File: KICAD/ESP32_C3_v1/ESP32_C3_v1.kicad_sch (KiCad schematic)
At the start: 1 part, among them U1 ESP32-C3-DevKitC-02

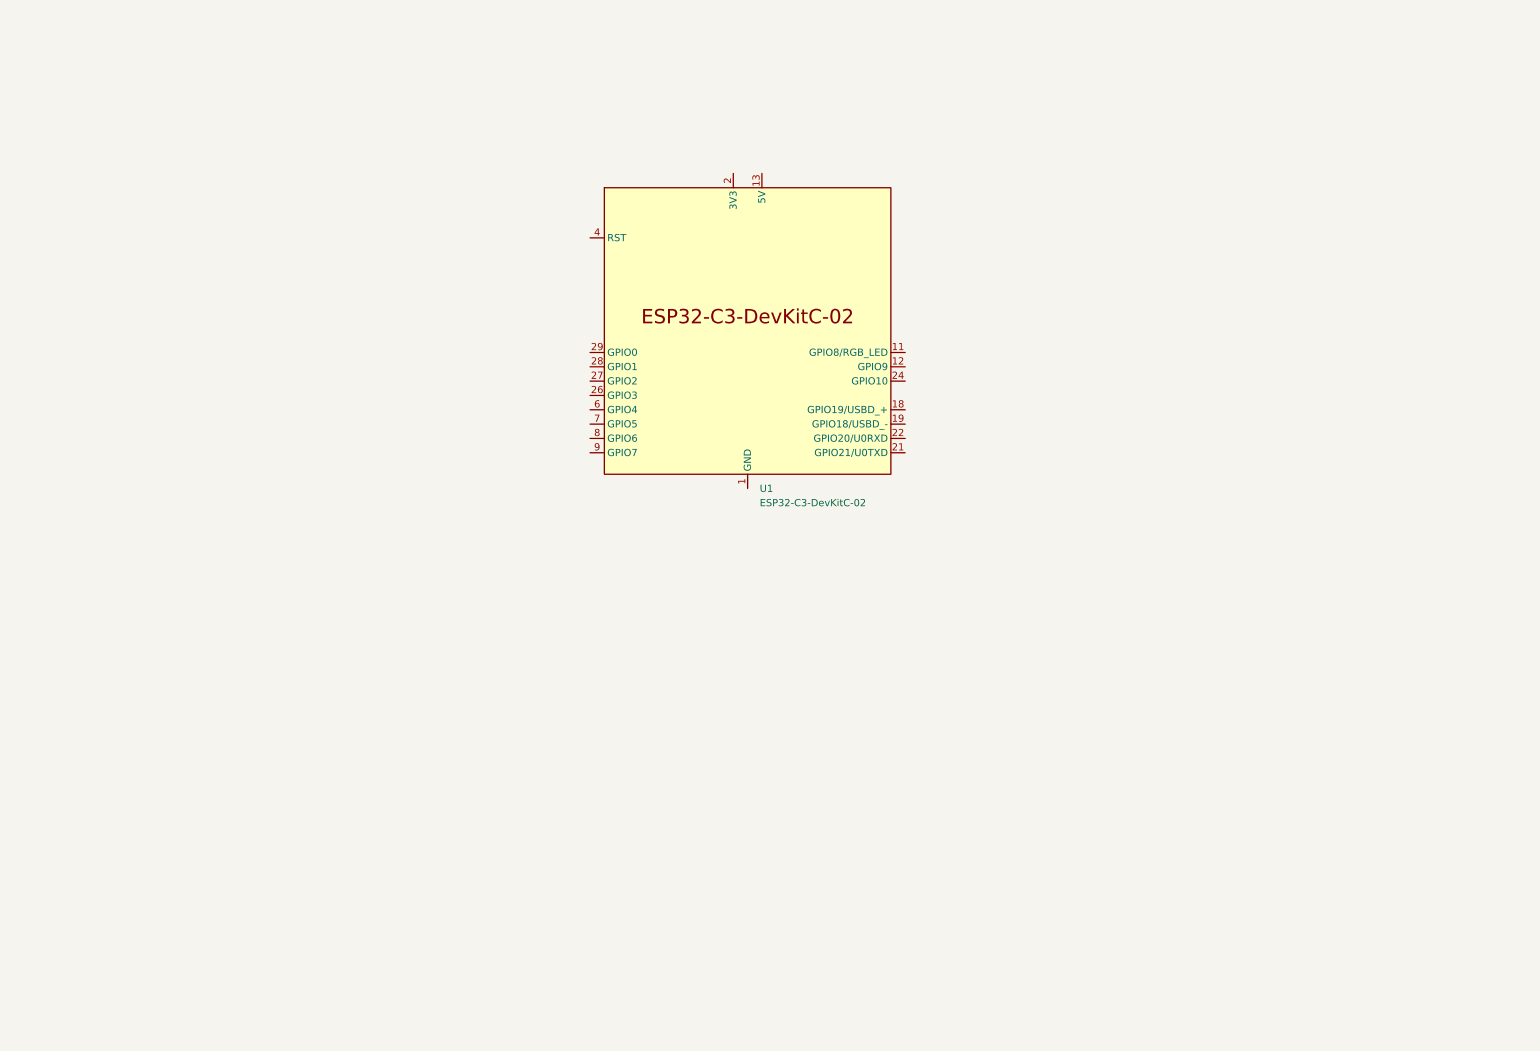
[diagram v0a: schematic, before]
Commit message: Add cleaned ESP32-C3 harness KiCad project
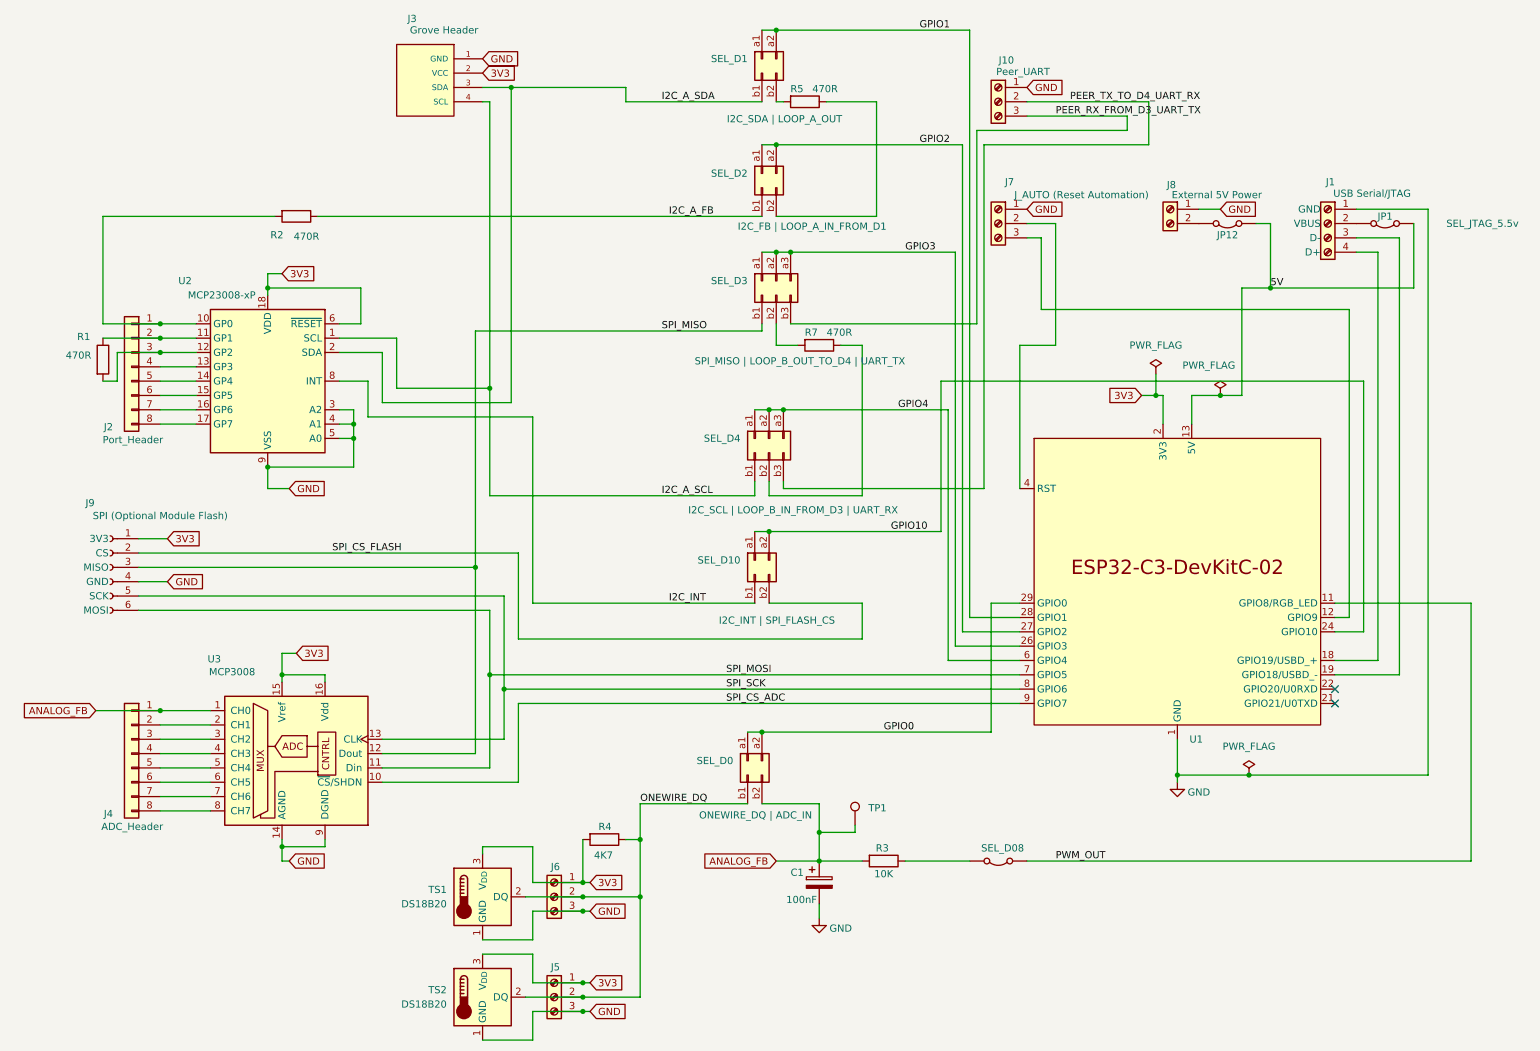
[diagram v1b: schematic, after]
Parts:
- removed U1: ESP32-C3-DevKitC-02, PCM_Espressif:ESP32-C3-DevKitC-02, symbol PCM_Espressif:ESP32-C3-DevKitC-02
- added C1: 100nF, ESP32_C3_Harness:C_Disc_D4.7mm_W2.5mm_P5.00mm, symbol ESP32_C3_Harness:C_Polarized
- added J1: USB Serial/JTAG, ESP32_C3_Harness:TerminalBlock_Phoenix_MPT-0,5-4-2.54_1x04_P2.54mm_Horizontal, symbol ESP32_C3_Harness:Screw_Terminal_01x04
- added J10: Peer_UART, ESP32_C3_Harness:TerminalBlock_Phoenix_MPT-0,5-3-2.54_1x03_P2.54mm_Horizontal, symbol ESP32_C3_Harness:Screw_Terminal_01x03
- added J2: Port_Header, ESP32_C3_Harness:PinHeader_1x08_P2.54mm_Vertical, symbol ESP32_C3_Harness:Conn_01x08
- added J3: Grove Header, ESP32_C3_Harness:Grove_1x04_P2mm(SEEED_110990030), symbol ESP32_C3_Harness:Grove_Female_Header_-_DIP-4P-2.0mm
- added J4: ADC_Header, ESP32_C3_Harness:PinHeader_1x08_P2.54mm_Vertical, symbol ESP32_C3_Harness:Conn_01x08
- added J5, J6: Screw_Terminal_01x03, ESP32_C3_Harness:TerminalBlock_Phoenix_MPT-0,5-3-2.54_1x03_P2.54mm_Horizontal, symbol ESP32_C3_Harness:Screw_Terminal_01x03
- added J7: J_AUTO (Reset Automation), ESP32_C3_Harness:TerminalBlock_Phoenix_MPT-0,5-3-2.54_1x03_P2.54mm_Horizontal, symbol ESP32_C3_Harness:Screw_Terminal_01x03
- added J8: External 5V Power, ESP32_C3_Harness:TerminalBlock_Phoenix_MPT-0,5-2-2.54_1x02_P2.54mm_Horizontal, symbol ESP32_C3_Harness:Screw_Terminal_01x02
- added J9: SPI (Optional Module Flash), ESP32_C3_Harness:PinSocket_1x06_P2.54mm_Vertical, symbol ESP32_C3_Harness:Conn_01x06_Socket
- added JP1: SEL_JTAG_5.5v, ESP32_C3_Harness:PinHeader_1x02_P2.54mm_Vertical, symbol ESP32_C3_Harness:Jumper_2_Open
- added JP12: EXT_5V_SHUNT, ESP32_C3_Harness:PinHeader_1x02_P2.54mm_Vertical, symbol ESP32_C3_Harness:Jumper_2_Open
- added R1, R2, R5, R7: 470R, ESP32_C3_Harness:R_Axial_DIN0411_L9.9mm_D3.6mm_P5.08mm_Vertical, symbol ESP32_C3_Harness:Resistor
- added R3: 10K, ESP32_C3_Harness:R_Axial_DIN0411_L9.9mm_D3.6mm_P5.08mm_Vertical, symbol ESP32_C3_Harness:Resistor
- added R4: 4K7, ESP32_C3_Harness:R_Axial_DIN0411_L9.9mm_D3.6mm_P5.08mm_Vertical, symbol ESP32_C3_Harness:Resistor
- added SEL_D0: ONEWIRE_DQ | ADC_IN, ESP32_C3_Harness:PinHeader_2x02_P2.54mm_Vertical, symbol ESP32_C3_Harness:Conn_02x02_Row_Letter_First
- added SEL_D08: PWM_OUT, ESP32_C3_Harness:PinHeader_1x02_P2.54mm_Vertical, symbol ESP32_C3_Harness:Jumper_2_Open
- added SEL_D1: I2C_SDA | LOOP_A_OUT, ESP32_C3_Harness:PinHeader_2x02_P2.54mm_Vertical, symbol ESP32_C3_Harness:Conn_02x02_Row_Letter_First
- added SEL_D10: I2C_INT | SPI_FLASH_CS, ESP32_C3_Harness:PinHeader_2x02_P2.54mm_Vertical, symbol ESP32_C3_Harness:Conn_02x02_Row_Letter_First
- added SEL_D2: I2C_FB | LOOP_A_IN_FROM_D1, ESP32_C3_Harness:PinHeader_2x02_P2.54mm_Vertical, symbol ESP32_C3_Harness:Conn_02x02_Row_Letter_First
- added SEL_D3: SPI_MISO | LOOP_B_OUT_TO_D4 | UART_TX, ESP32_C3_Harness:PinHeader_2x03_P2.54mm_Vertical, symbol ESP32_C3_Harness:Conn_02x03_Row_Letter_First
- added SEL_D4: I2C_SCL | LOOP_B_IN_FROM_D3 | UART_RX, ESP32_C3_Harness:PinHeader_2x03_P2.54mm_Vertical, symbol ESP32_C3_Harness:Conn_02x03_Row_Letter_First
- added TP1: ANALOG_FB, ESP32_C3_Harness:PinHeader_1x01_P2.54mm_Vertical, symbol ESP32_C3_Harness:TestPoint
- added TS1, TS2: DS18B20, Package_TO_SOT_THT:TO-92_Inline, symbol ESP32_C3_Harness:DS18B20
- added U1: ESP32-C3-DevKitC-02, ESP32_C3_Harness:ESP32-C3-DevKitC-02, symbol ESP32_C3_Harness:ESP32-C3-DevKitC-02
- added U2: MCP23008-xP, ESP32_C3_Harness:DIP-18_W7.62mm, symbol ESP32_C3_Harness:MCP23008-xP
- added U3: MCP3008, ESP32_C3_Harness:DIP-16_W7.62mm, symbol ESP32_C3_Harness:MCP3008
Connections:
- net 3V3: now also J3.2 (VCC), J5.1 (Pin_1), J6.1 (Pin_1), J9.1 (3V3), R4.2, TS1.3 (V_{DD}), TS2.3 (V_{DD}), U1.2 (3V3), U1.3 (3V3), U2.18 (VDD), U2.6 (~{RESET}), U3.15 (Vref), U3.16 (Vdd)
- net 5V: now also JP1.1 (A), JP12.1 (A), U1.13 (5V), U1.14 (5V)
- new net: J1.2 (VBUS), JP1.2 (B)
- new net: J1.3 (D-), U1.19 (GPIO18/USBD_-)
- new net: J1.4 (D+), U1.18 (GPIO19/USBD_+)
- new net: R7.2, SEL_D3.b2 (Pin_b2)
- new net: J2.2 (Pin_2), R1.1, U2.11 (GP1)
- new net: J2.3 (Pin_3), R1.2, U2.12 (GP2)
- new net: R5.1, SEL_D2.b2 (Pin_b2)
- new net: R5.2, SEL_D1.b2 (Pin_b2)
- new net: R7.1, SEL_D4.b2 (Pin_b2)
- new net: J2.1 (Pin_1), R2.2, U2.10 (GP0)
- new net: J2.4 (Pin_4), U2.13 (GP3)
- new net: J2.5 (Pin_5), U2.14 (GP4)
- new net: J2.6 (Pin_6), U2.15 (GP5)
- new net: J2.7 (Pin_7), U2.16 (GP6)
- new net: J2.8 (Pin_8), U2.17 (GP7)
- new net: J4.2 (Pin_2), U3.2 (CH1)
- new net: J4.3 (Pin_3), U3.3 (CH2)
- new net: J4.4 (Pin_4), U3.4 (CH3)
- new net: J4.5 (Pin_5), U3.5 (CH4)
- new net: J4.6 (Pin_6), U3.6 (CH5)
- new net: J4.7 (Pin_7), U3.7 (CH6)
- new net: J4.8 (Pin_8), U3.8 (CH7)
- new net: R3.1, SEL_D08.2 (B)
- new net: J7.3 (Pin_3), U1.12 (GPIO9)
- new net: J7.2 (Pin_2), U1.4 (RST)
- new net: J8.2 (Pin_2), JP12.2 (B)
- new net ANALOG_FB: C1.1, J4.1 (Pin_1), R3.2, SEL_D0.b2 (Pin_b2), TP1.1, U3.1 (CH0)
- new net GND: C1.2, J1.1 (GND), J10.1 (Pin_1), J3.1 (GND), J5.3 (Pin_3), J6.3 (Pin_3), J7.1 (Pin_1), J8.1 (Pin_1), J9.4 (GND), TS1.1 (GND), TS2.1 (GND), U1.1 (GND), U1.10 (GND), U1.15 (GND), U1.16 (GND), U1.17 (GND), U1.20 (GND), U1.23 (GND), U1.25 (GND), U1.30 (GND), U1.5 (GND), U2.3 (A2), U2.4 (A1), U2.5 (A0), U2.9 (VSS), U3.14 (AGND), U3.9 (DGND)
- new net GPIO0: SEL_D0.a1 (Pin_a1), SEL_D0.a2 (Pin_a2), U1.29 (GPIO0)
- new net GPIO1: SEL_D1.a1 (Pin_a1), SEL_D1.a2 (Pin_a2), U1.28 (GPIO1)
- new net GPIO10: SEL_D10.a1 (Pin_a1), SEL_D10.a2 (Pin_a2), U1.24 (GPIO10)
- new net GPIO2: SEL_D2.a1 (Pin_a1), SEL_D2.a2 (Pin_a2), U1.27 (GPIO2)
- new net GPIO3: SEL_D3.a1 (Pin_a1), SEL_D3.a2 (Pin_a2), SEL_D3.a3 (Pin_a3), U1.26 (GPIO3)
- new net GPIO4: SEL_D4.a1 (Pin_a1), SEL_D4.a2 (Pin_a2), SEL_D4.a3 (Pin_a3), U1.6 (GPIO4)
- new net I2C_A_FB: R2.1, SEL_D2.b1 (Pin_b1)
- new net I2C_A_SCL: J3.4 (SCL), SEL_D4.b1 (Pin_b1), U2.1 (SCL)
- new net I2C_A_SDA: J3.3 (SDA), SEL_D1.b1 (Pin_b1), U2.2 (SDA)
- new net I2C_INT: SEL_D10.b1 (Pin_b1), U2.8 (INT)
- new net ONEWIRE_DQ: J5.2 (Pin_2), J6.2 (Pin_2), R4.1, SEL_D0.b1 (Pin_b1), TS1.2 (DQ), TS2.2 (DQ)
- new net PEER_RX_FROM_D3_UART_TX: J10.3 (Pin_3), SEL_D3.b3 (Pin_b3)
- new net PEER_TX_TO_D4_UART_RX: J10.2 (Pin_2), SEL_D4.b3 (Pin_b3)
- new net PWM_OUT: SEL_D08.1 (A), U1.11 (GPIO8/RGB_LED)
- new net SPI_CS_ADC: U1.9 (GPIO7), U3.10 (~{CS}/SHDN)
- new net SPI_CS_FLASH: J9.2 (CS), SEL_D10.b2 (Pin_b2)
- new net SPI_MISO: J9.3 (MISO), SEL_D3.b1 (Pin_b1), U3.12 (Dout)
- new net SPI_MOSI: J9.6 (MOSI), U1.7 (GPIO5), U3.11 (Din)
- new net SPI_SCK: J9.5 (SCK), U1.8 (GPIO6), U3.13 (CLK)
- no-connect marks 0 -> 2
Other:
- company: (none) -> SimonGAndrews
- title: (none) -> Espruino ESP32_C3 Test Harness

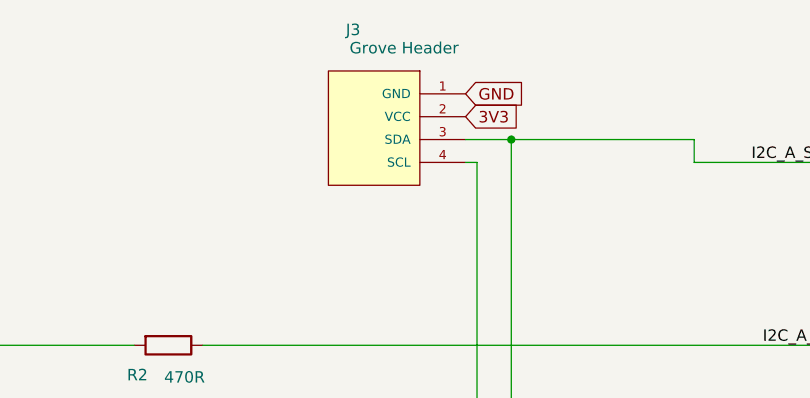
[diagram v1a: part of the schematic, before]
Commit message: Add ESP32-C3 harness v1 PCB draft
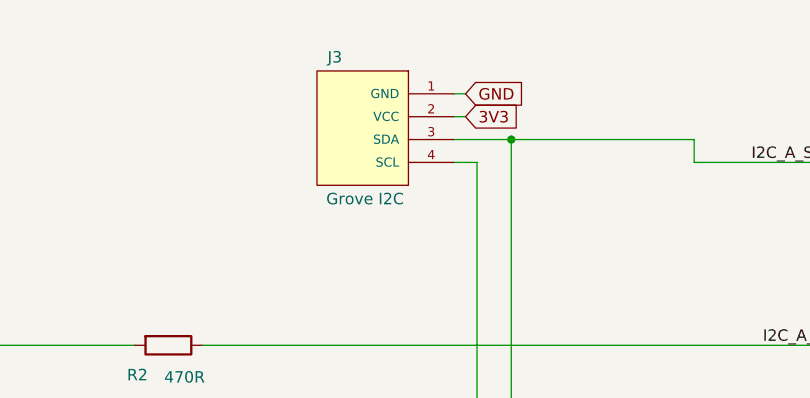
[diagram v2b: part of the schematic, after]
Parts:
- J3: value Grove Header -> Grove I2C
- JP12: value EXT_5V_SHUNT -> EXT_5V
- SEL_D0, SEL_D1, SEL_D10, SEL_D2: footprint ESP32_C3_Harness:PinHeader_2x02_P2.54mm_Vertical -> ESP32_C3_Harness:PinHeader_2x02_RowLetter_P2.54mm_Vertical
- SEL_D3, SEL_D4: footprint ESP32_C3_Harness:PinHeader_2x03_P2.54mm_Vertical -> ESP32_C3_Harness:PinHeader_2x03_RowLetter_P2.54mm_Vertical
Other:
- moved on the sheet: J3
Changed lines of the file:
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@@
 	(wire
 		(pts
+			(xy 96.52 21.59) (xy 97.79 21.59)
+		)
+		(stroke
+			(width 0)
+			(type default)
+		)
+	)
+	(wire
+		(pts
 			(xy 62.23 128.27) (xy 62.23 129.54)
 		)
@@
 	(wire
 		(pts
-			(xy 97.79 26.67) (xy 99.06 26.67)
+			(xy 96.52 26.67) (xy 99.06 26.67)
 		)
 		(stroke
@@
 	(wire
 		(pts
+			(xy 96.52 19.05) (xy 97.79 19.05)
+		)
+		(stroke
+			(width 0)
+			(type default)
+		)
+	)
+	(wire
+		(pts
 			(xy 232.41 59.69) (xy 237.49 59.69)
 		)
@@
 	(wire
 		(pts
-			(xy 97.79 24.13) (xy 102.87 24.13)
+			(xy 96.52 24.13) (xy 102.87 24.13)
 		)
 		(stroke
@@
 			)
 		)
-		(property "Footprint" "ESP32_C3_Harness:PinHeader_2x03_P2.54mm_Vertical"
+		(property "Footprint" "ESP32_C3_Harness:PinHeader_2x03_RowLetter_P2.54mm_Vertical"
 			(at 149.86 58.42 0)
 			(effects
@@
 			)
 		)
-		(property "Footprint" "ESP32_C3_Harness:PinHeader_2x02_P2.54mm_Vertical"
+		(property "Footprint" "ESP32_C3_Harness:PinHeader_2x02_RowLetter_P2.54mm_Vertical"
 			(at 147.32 39.37 0)
 			(effects
@@
 			)
 		)
-		(property "Footprint" "ESP32_C3_Harness:PinHeader_2x02_P2.54mm_Vertical"
+		(property "Footprint" "ESP32_C3_Harness:PinHeader_2x02_RowLetter_P2.54mm_Vertical"
 			(at 147.32 19.05 0)
 			(effects
@@
 			)
 		)
-		(property "Footprint" "ESP32_C3_Harness:PinHeader_2x03_P2.54mm_Vertical"
+		(property "Footprint" "ESP32_C3_Harness:PinHeader_2x03_RowLetter_P2.54mm_Vertical"
 			(at 148.59 86.36 0)
 			(effects
@@
 			)
 		)
-		(property "Footprint" "ESP32_C3_Harness:PinHeader_2x02_P2.54mm_Vertical"
+		(property "Footprint" "ESP32_C3_Harness:PinHeader_2x02_RowLetter_P2.54mm_Vertical"
 			(at 144.78 143.51 0)
 			(effects
@@
 	(symbol
 		(lib_id "ESP32_C3_Harness:Grove_Female_Header_-_DIP-4P-2.0mm")
-		(at 87.63 21.59 0)
+		(at 86.36 21.59 0)
 		(mirror y)
 		(unit 1)
@@
 		(dnp no)
 		(property "Reference" "J3"
-			(at 86.106 11.938 0)
+			(at 84.074 14.986 0)
 			(effects
 				(font
@@
 			)
 		)
-		(property "Value" "Grove Header"
-			(at 97.028 13.97 0)
+		(property "Value" "Grove I2C"
+			(at 90.932 30.734 0)
 			(effects
 				(font
@@
 		)
 		(property "Footprint" "ESP32_C3_Harness:Grove_1x04_P2mm(SEEED_110990030)"
-			(at 87.122 8.382 0)
+			(at 85.852 8.382 0)
 			(effects
 				(font
@@
 		)
 		(property "Datasheet" "https://www.snapeda.com/parts/110990030%2010PCS/PACK/Seeed+Studio/view-part/?ref=snap"
-			(at 53.086 12.954 0)
+			(at 51.816 12.954 0)
 			(effects
 				(font
@@
 		)
 		(property "Description" "Grove_Female_Header  DIP-4P-2.0mm"
-			(at 80.772 10.668 0)
+			(at 79.502 10.668 0)
 			(effects
 				(font
@@
 			)
 		)
-		(property "Value" "EXT_5V_SHUNT"
+		(property "Value" "EXT_5V"
 			(at 229.87 39.37 90)
 			(effects
@@
 			)
 		)
-		(property "Footprint" "ESP32_C3_Harness:PinHeader_2x02_P2.54mm_Vertical"
+		(property "Footprint" "ESP32_C3_Harness:PinHeader_2x02_RowLetter_P2.54mm_Vertical"
 			(at 146.05 107.95 0)
 			(effects
